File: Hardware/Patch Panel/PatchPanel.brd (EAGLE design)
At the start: 226 x 119 mm, 49 parts

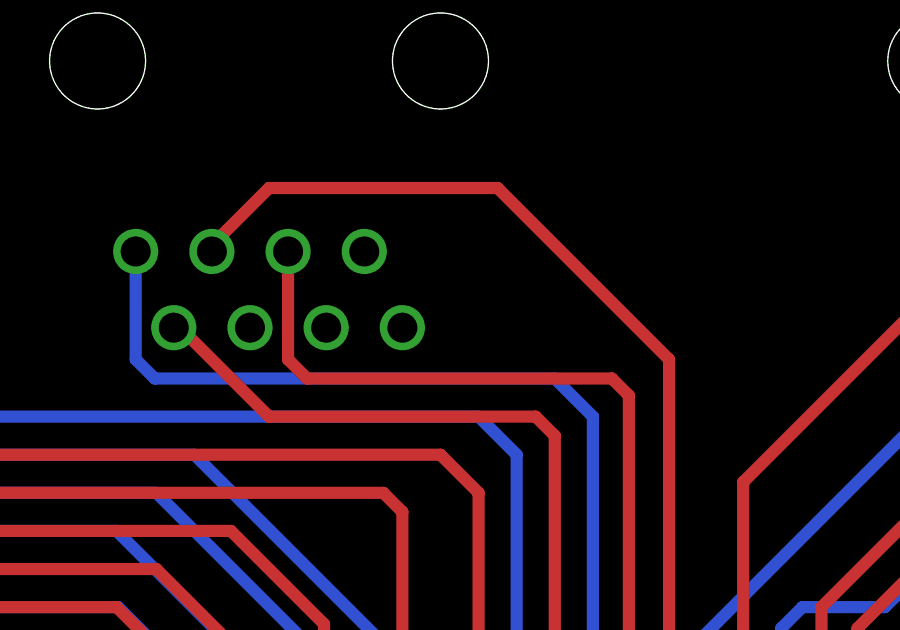
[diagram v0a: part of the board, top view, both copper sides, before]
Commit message: Issue #49 Patch Panel RJ-45 port number 5 Fixed the incorrect wires on board file and schematic file.
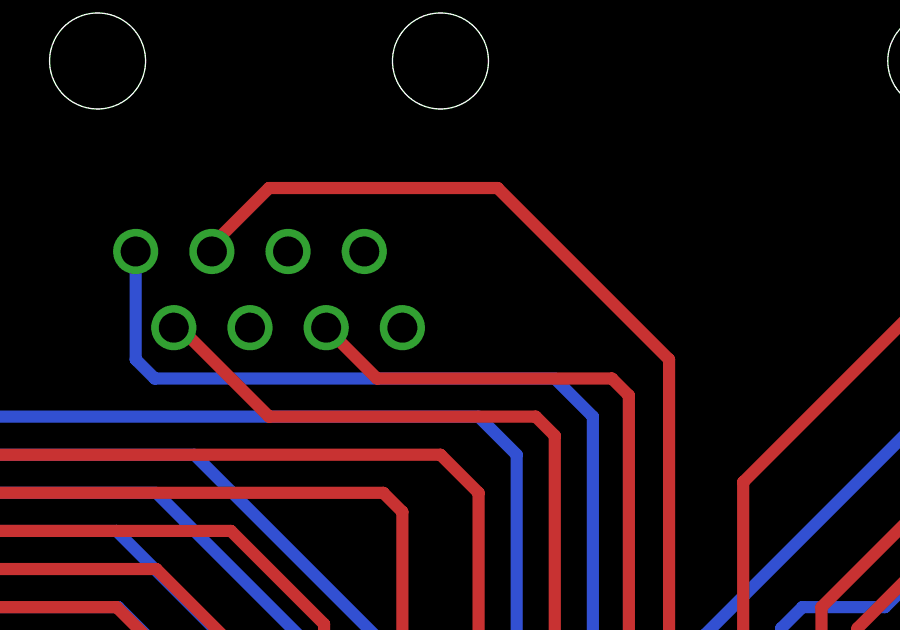
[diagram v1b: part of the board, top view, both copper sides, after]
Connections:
- net 5_TX-: now also RS-485_OUT5.6; no longer RS-485_OUT5.5
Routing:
- net 5_TX-: track 27.5 -> 23.0 mm
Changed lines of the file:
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@@
 <?xml version="1.0" encoding="utf-8"?>
 <!DOCTYPE eagle SYSTEM "eagle.dtd">
-<eagle version="6.2">
+<eagle version="6.5.0">
 <drawing>
 <settings>
@@
 </class>
 </classes>
-<designrules>
+<designrules name="default">
 <description language="de">&lt;b&gt;EAGLE Design Rules&lt;/b&gt;
 &lt;p&gt;
@@
 <signal name="5_TX-">
 <contactref element="U$1" pad="18"/>
-<contactref element="RS-485_OUT5" pad="5"/>
-<wire x1="99.695" y1="93.135" x2="99.695" y2="89.535" width="0.4064" layer="1"/>
-<wire x1="99.695" y1="89.535" x2="100.33" y2="88.9" width="0.4064" layer="1"/>
-<wire x1="100.33" y1="88.9" x2="110.49" y2="88.9" width="0.4064" layer="1"/>
+<wire x1="102.66" y1="88.9" x2="110.49" y2="88.9" width="0.4064" layer="1"/>
 <wire x1="110.49" y1="88.9" x2="111.055" y2="88.335" width="0.4064" layer="1"/>
 <wire x1="111.055" y1="88.335" x2="111.055" y2="76.3225" width="0.4064" layer="1"/>
+<contactref element="RS-485_OUT5" pad="6"/>
+<wire x1="102.66" y1="88.9" x2="100.965" y2="90.595" width="0.4064" layer="1"/>
 </signal>
 <signal name="5_RX+">
@@
 </board>
 </drawing>
+<compatibility>
+<note version="6.3" minversion="6.2.2" severity="warning">
+Since Version 6.2.2 text objects can contain more than one line,
+which will not be processed correctly with this version.
+</note>
+</compatibility>
 </eagle>
